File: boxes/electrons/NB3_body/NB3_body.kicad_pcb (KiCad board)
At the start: 2 copper layers, 200 x 199.5 mm, 41 parts, among them J1 Conn_02x05_Counter_Clockwise, J10 JST SH 4-way Socket, J12 Conn_02x03_Top_Bottom, J13 Conn_02x03_Top_Bottom, J14 Conn_02x05_Counter_Clockwise, J15 Conn_02x05_Counter_Clockwise, J2 Conn_02x05_Counter_Clockwise, J3 Conn_02x05_Counter_Clockwise, J4 Conn_02x05_Counter_Clockwise, J5 Conn_02x05_Counter_Clockwise, J6 Conn_02x05_Counter_Clockwise, J7 Conn_02x07_Odd_Even, J8 Conn_02x07_Odd_Even, J9 Conn_02x07_Odd_Even

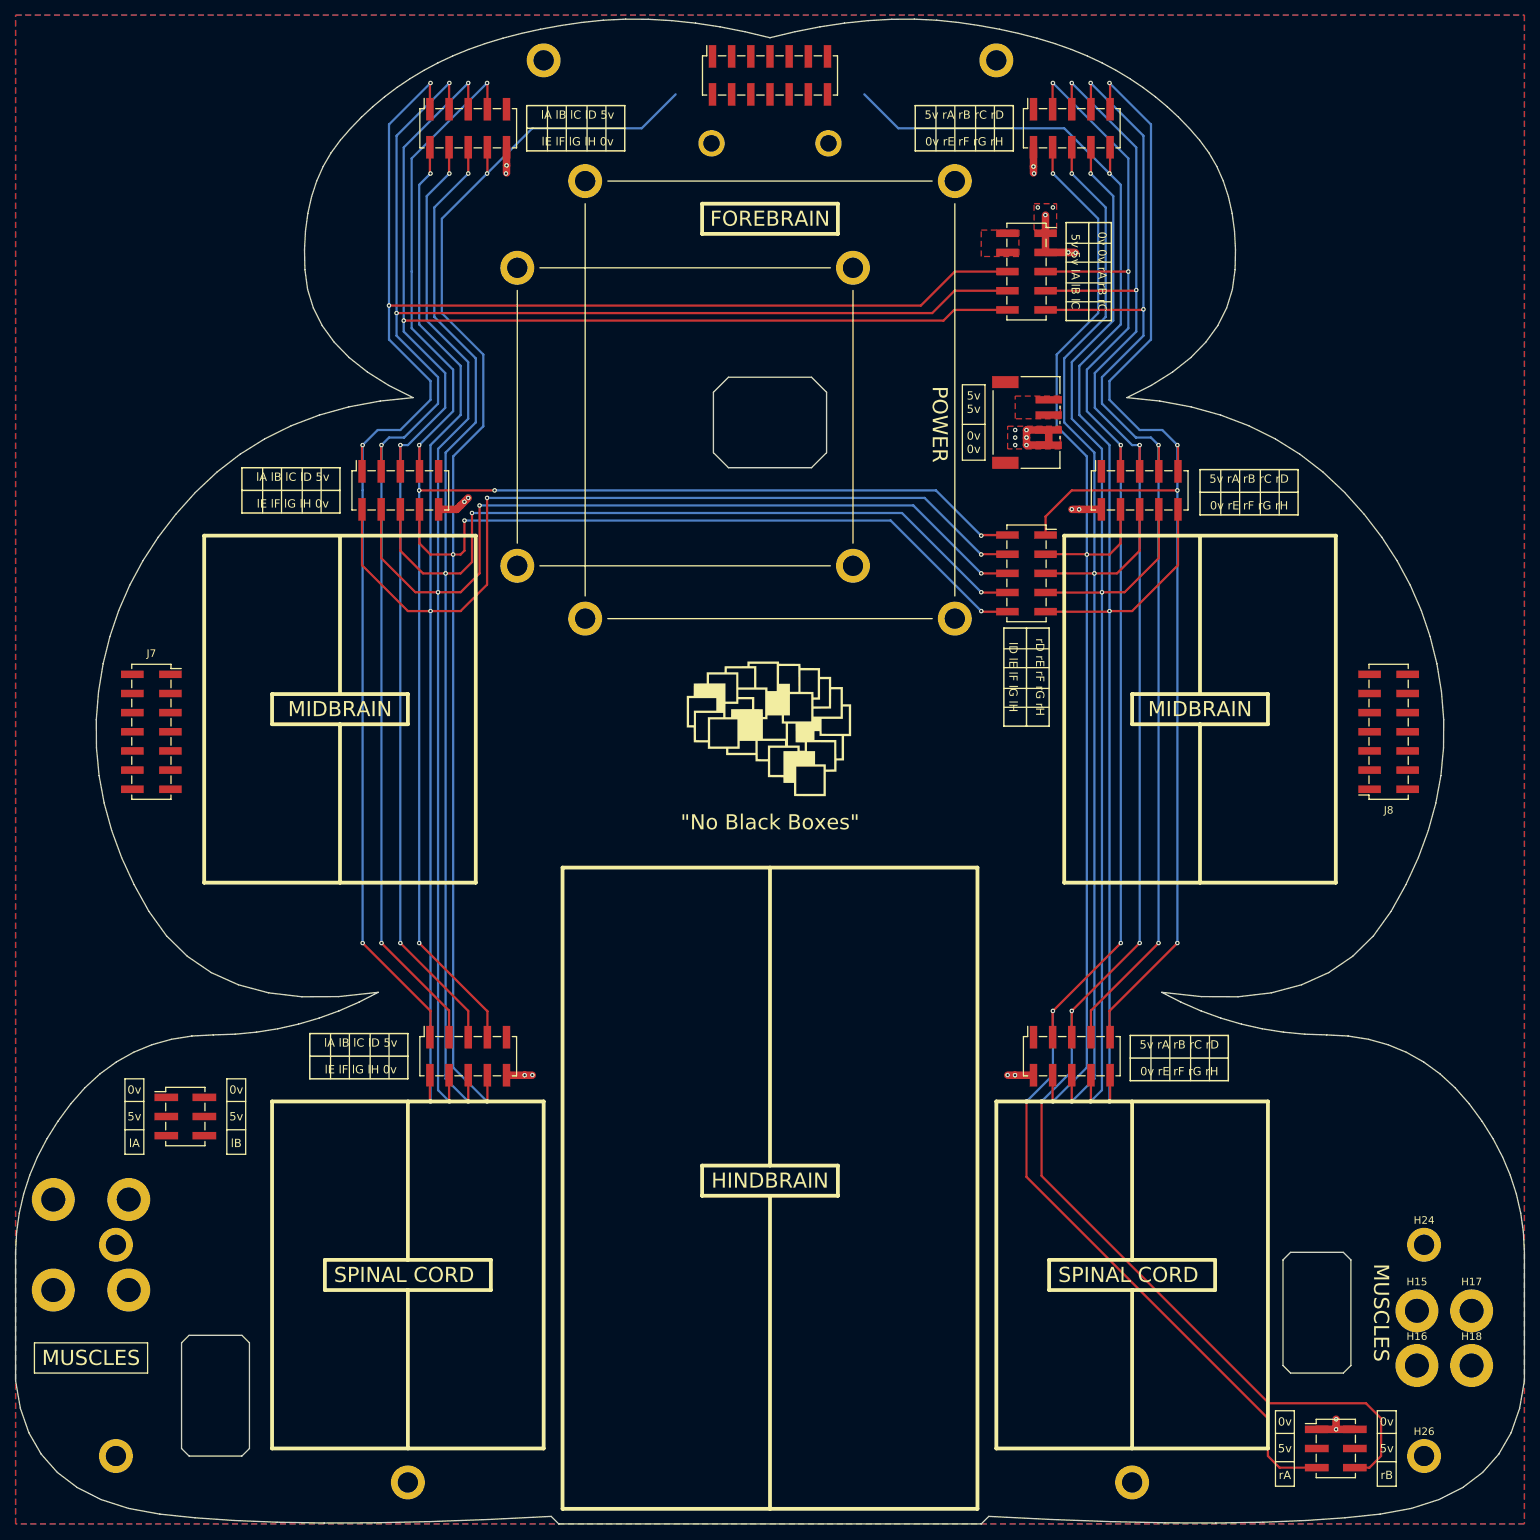
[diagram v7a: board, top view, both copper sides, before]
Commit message: Updated NB3 body (v4) - ear/mouth and TT motors
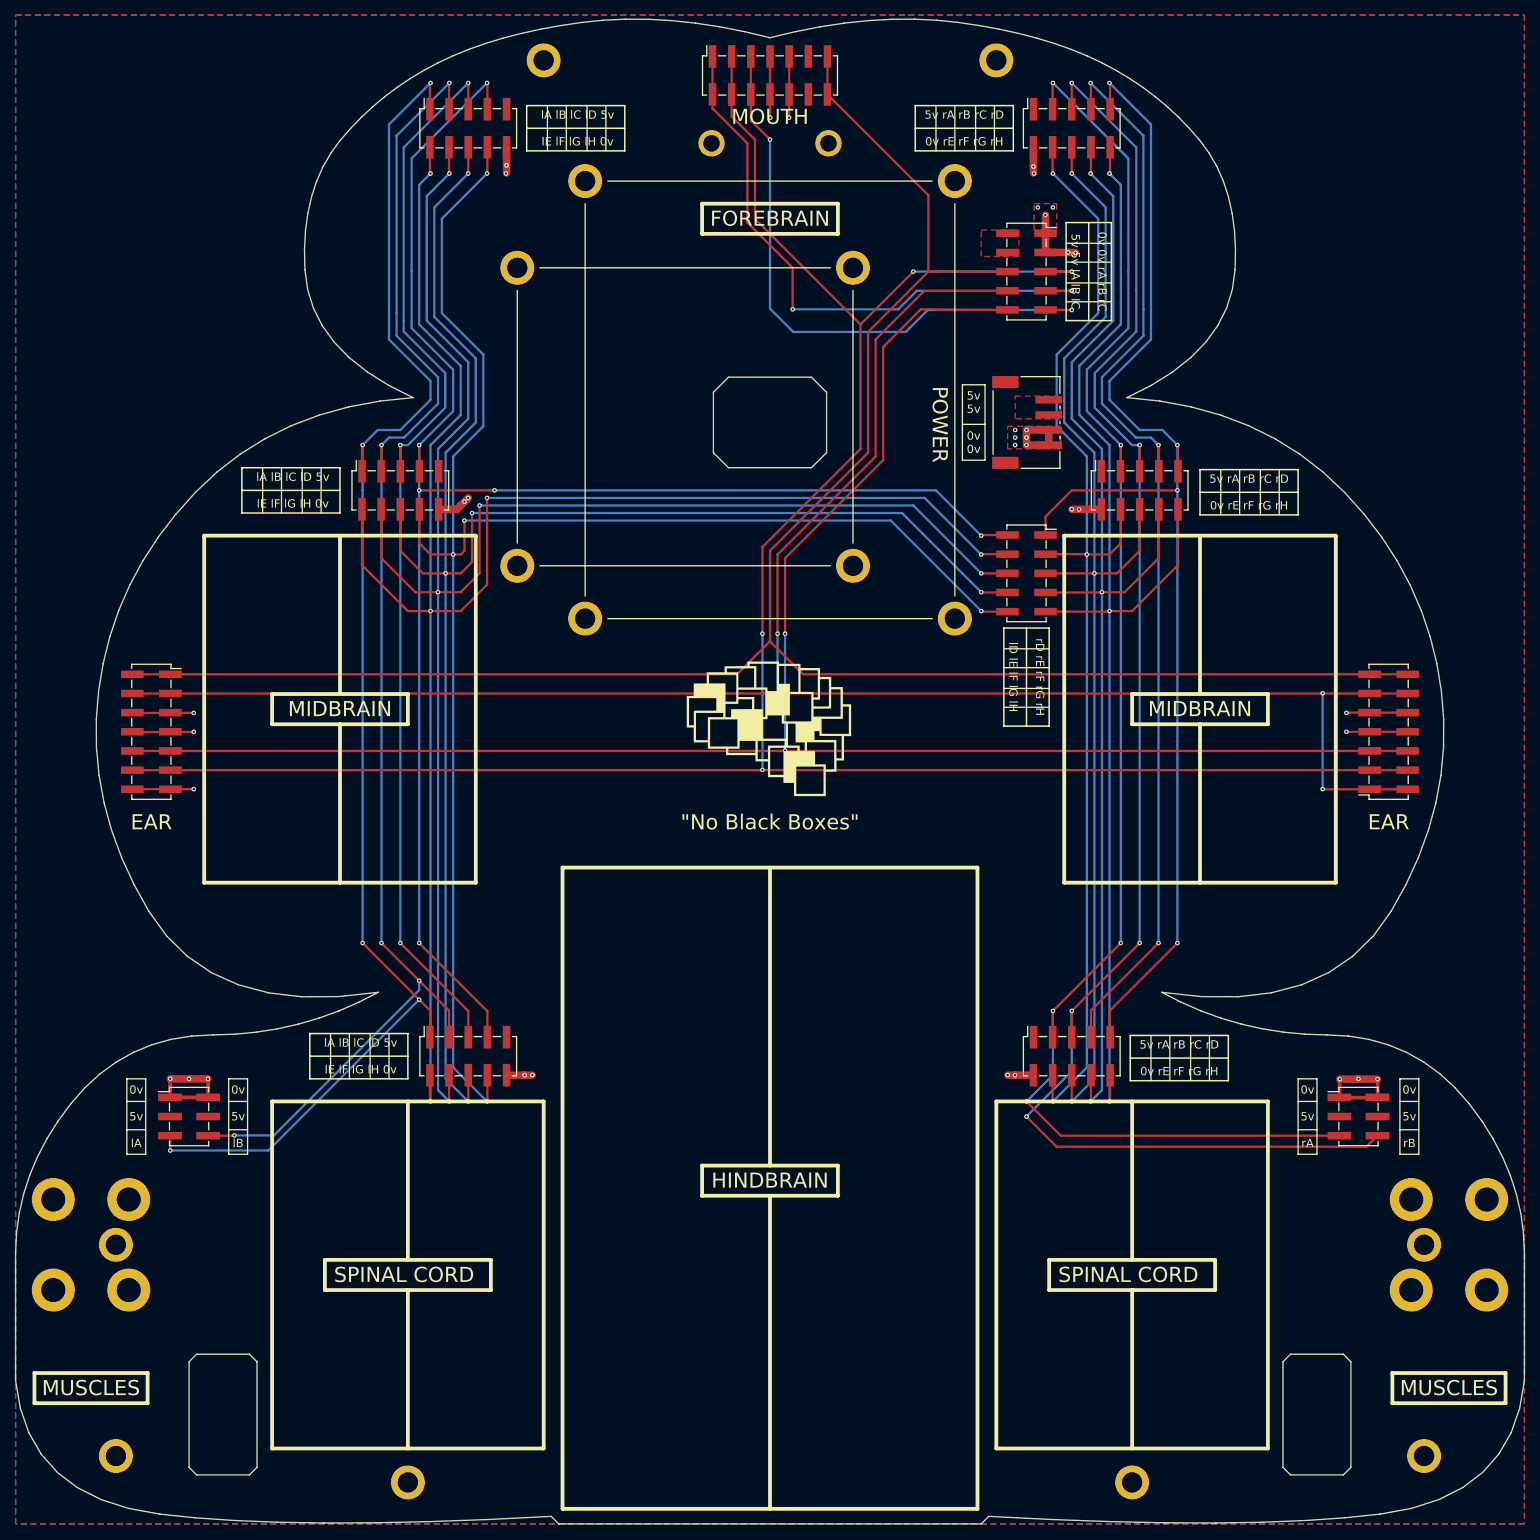
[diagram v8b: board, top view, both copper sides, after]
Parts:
- moved J13 44.1 mm to (202.5, 169.0)
- moved H17 14.9 mm to (219.5, 180.0)
- moved H15 14.8 mm to (209.5, 180.0)
- moved H18 10.2 mm to (219.5, 192.0)
- moved H16 10.0 mm to (209.5, 192.0)
- moved J12 0.50 mm to (47.5, 169.0)
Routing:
- net /WS: track 0.00 -> 310.4 mm, vias 0 -> 4
- net /SCK: track 0.00 -> 274.9 mm
- net +3V3: track 0.00 -> 265.6 mm, vias 0 -> 4
- net /SDI: track 0.00 -> 246.5 mm, vias 0 -> 2
- net /LC: track 226.7 -> 146.0 mm, vias 4 -> 3
- net /SDO: track 0.00 -> 80.4 mm, vias 0 -> 2
- net GND: track 47.6 -> 128.0 mm, vias 25 -> 36
- net /GAIN: track 0.00 -> 79.4 mm, vias 0 -> 2
- net /LB: track 228.9 -> 183.9 mm, vias 4 -> 5
- net /LA: track 231.2 -> 190.6 mm, vias 4 -> 5
- net /RB: track 249.0 -> 211.3 mm, vias 6 -> 5
- net /RH: track 198.9 -> 162.1 mm
- net /RA: track 237.3 -> 202.3 mm, vias 6 -> 5
- net /LH: track 259.9 -> 230.6 mm
- net /RC: track 159.7 -> 146.6 mm, vias 4 -> 3
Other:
- outline, holes or cut-outs redrawn
- board text added: "EAR"
- board text added: "MOUTH"
- board text added: "Speaker"
